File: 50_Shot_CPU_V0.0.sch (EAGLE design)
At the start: 75 parts, among them IC1 PIC24FJ128GA010, IC2 93LC46ST, J1 J12, J12 A311422_nd, J13 22-23-2021, J14 22-23-2021, J3 22-23-2021, J4 22-23-2021, J5 22-23-2021, Q1 Qs5U34CT-ND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

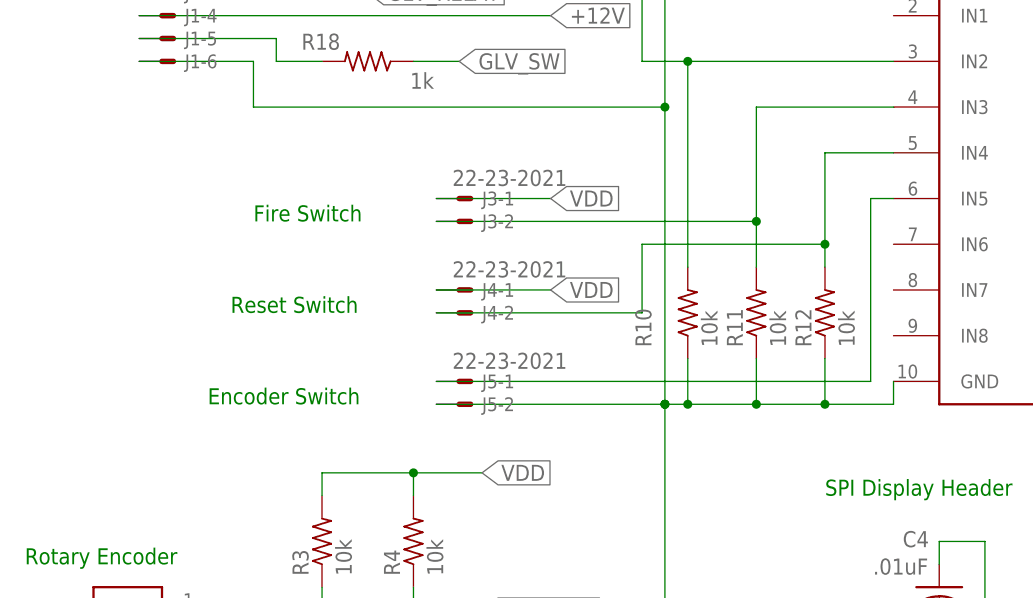
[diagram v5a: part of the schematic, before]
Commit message: Added fire/reset/encoder switches
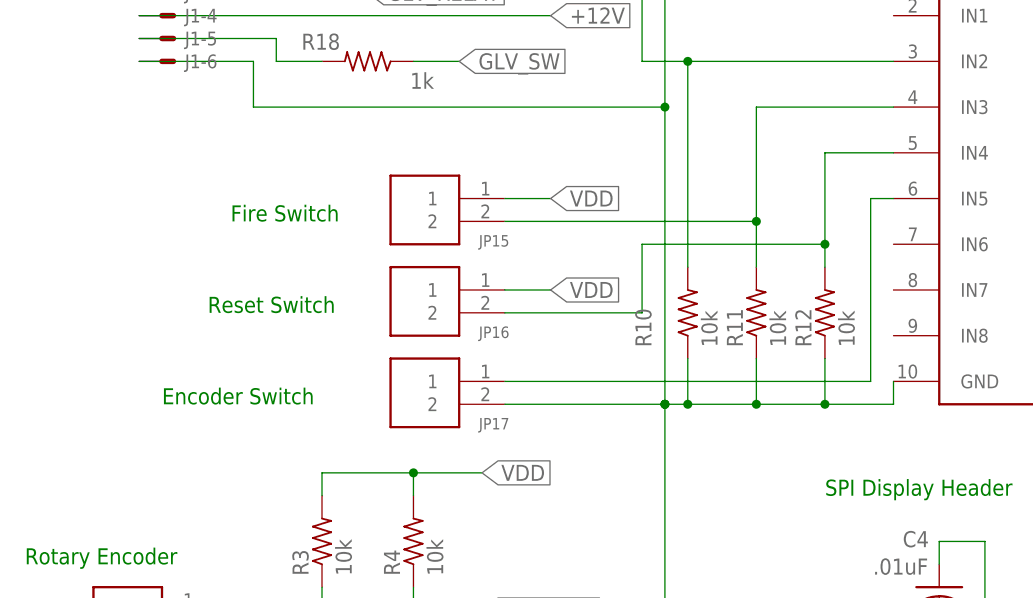
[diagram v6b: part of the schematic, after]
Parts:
- removed J3, J4, J5: 22-23-2021, Mine:22-23-2021
- added JP15, JP16, JP17: SHERLOCK_2PIN_RGT, Mine:SHERLOCK_2PIN_RGT
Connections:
- net GND: now also JP17.2; no longer J5-2.S
- net N$58: now also JP15.2; no longer J3-2.S
- net N$7: now also JP17.1; no longer J5-1.S
- net N$8: now also JP16.2; no longer J4-2.S
- net VDD: now also JP15.1, JP16.1; no longer J3-1.S, J4-1.S
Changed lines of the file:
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@@
 <part name="U1" library="Mine" deviceset="MAX6818" device="" value="MAX6818"/>
 <part name="C5" library="rcl" deviceset="C-US" device="C0805" value="1uF"/>
-<part name="J4" library="Mine" deviceset="22-23-2021" device=""/>
 <part name="R12" library="rcl" deviceset="R-US_" device="M0805" value="10k"/>
 <part name="SUPPLY4" library="supply2" deviceset="GND" device=""/>
-<part name="J5" library="Mine" deviceset="22-23-2021" device=""/>
 <part name="R11" library="rcl" deviceset="R-US_" device="M0805" value="10k"/>
 <part name="U2" library="Texas Instruments_By_element14_Batch_1" deviceset="LP2985A-33DBVTE4" device=""/>
@@
 <part name="D2" library="semicon-smd-ipc" deviceset="D-" device="SOD-80" value="LL4148FSCT-ND"/>
 <part name="SUPPLY2" library="supply2" deviceset="GND" device=""/>
-<part name="J3" library="Mine" deviceset="22-23-2021" device=""/>
 <part name="R10" library="rcl" deviceset="R-US_" device="M0805" value="10k"/>
 <part name="J12" library="Mine" deviceset="RJ_25" device="" value="A311422_nd"/>
@@
 <part name="JP13" library="Mine" deviceset="SHERLOCK_8PIN_RGT" device=""/>
 <part name="JP14" library="Mine" deviceset="SHERLOCK_6PIN_RGT" device=""/>
+<part name="JP15" library="Mine" deviceset="SHERLOCK_2PIN_RGT" device=""/>
+<part name="JP16" library="Mine" deviceset="SHERLOCK_2PIN_RGT" device=""/>
+<part name="JP17" library="Mine" deviceset="SHERLOCK_2PIN_RGT" device=""/>
 </parts>
 <sheets>
@@
 <text x="-22.86" y="86.36" size="1.778" layer="91">Circuit Board Header</text>
 <text x="-53.34" y="198.12" size="1.778" layer="91">I2C Header</text>
-<text x="-144.78" y="109.22" size="1.778" layer="91">Fire Switch</text>
-<text x="-147.32" y="99.06" size="1.778" layer="91">Reset Switch</text>
-<text x="-149.86" y="88.9" size="1.778" layer="91">Encoder Switch</text>
+<text x="-147.32" y="109.22" size="1.778" layer="91">Fire Switch</text>
+<text x="-149.86" y="99.06" size="1.778" layer="91">Reset Switch</text>
+<text x="-154.94" y="88.9" size="1.778" layer="91">Encoder Switch</text>
 <text x="-172.72" y="-17.78" size="1.778" layer="91">Firing Battery Measurement</text>
 <frame x1="-182.88" y1="-76.2" x2="276.86" y2="220.98" columns="8" rows="5" layer="91"/>
@@
 <attribute name="VALUE" x="-62.611" y="148.844" size="1.778" layer="96" rot="R270"/>
 </instance>
-<instance part="J4" gate="-1" x="-121.92" y="101.6" smashed="yes">
-<attribute name="NAME" x="-119.38" y="100.838" size="1.524" layer="95"/>
-<attribute name="VALUE" x="-122.682" y="102.997" size="1.778" layer="96"/>
-</instance>
-<instance part="J4" gate="-2" x="-121.92" y="99.06" smashed="yes">
-<attribute name="NAME" x="-119.38" y="98.298" size="1.524" layer="95"/>
-</instance>
 <instance part="R12" gate="G$1" x="-81.28" y="99.06" smashed="yes" rot="R90">
 <attribute name="NAME" x="-82.7786" y="95.25" size="1.778" layer="95" rot="R90"/>
@@
 <instance part="SUPPLY4" gate="GND" x="-99.06" y="-27.94" smashed="yes">
 <attribute name="VALUE" x="-100.965" y="-31.115" size="1.778" layer="96"/>
-</instance>
-<instance part="J5" gate="-1" x="-121.92" y="91.44" smashed="yes">
-<attribute name="NAME" x="-119.38" y="90.678" size="1.524" layer="95"/>
-<attribute name="VALUE" x="-122.682" y="92.837" size="1.778" layer="96"/>
-</instance>
-<instance part="J5" gate="-2" x="-121.92" y="88.9" smashed="yes">
-<attribute name="NAME" x="-119.38" y="88.138" size="1.524" layer="95"/>
 </instance>
 <instance part="R11" gate="G$1" x="-88.9" y="99.06" smashed="yes" rot="R90">
@@
 <attribute name="VALUE" x="-151.765" y="-8.255" size="1.778" layer="96"/>
 </instance>
-<instance part="J3" gate="-1" x="-121.92" y="111.76"/>
-<instance part="J3" gate="-2" x="-121.92" y="109.22"/>
 <instance part="R10" gate="G$1" x="-96.52" y="99.06" smashed="yes" rot="R90">
 <attribute name="NAME" x="-100.5586" y="95.25" size="1.778" layer="95" rot="R90"/>
@@
 <instance part="JP13" gate="G$1" x="238.76" y="147.32"/>
 <instance part="JP14" gate="G$1" x="238.76" y="119.38"/>
+<instance part="JP15" gate="G$1" x="-121.92" y="109.22" smashed="yes" rot="MR0">
+<attribute name="NAME" x="-116.332" y="106.426" size="1.27" layer="95" rot="MR0"/>
+</instance>
+<instance part="JP16" gate="G$1" x="-121.92" y="99.06" smashed="yes" rot="MR0">
+<attribute name="NAME" x="-116.332" y="96.266" size="1.27" layer="95" rot="MR0"/>
+</instance>
+<instance part="JP17" gate="G$1" x="-121.92" y="88.9" smashed="yes" rot="MR0">
+<attribute name="NAME" x="-116.332" y="86.106" size="1.27" layer="95" rot="MR0"/>
+</instance>
 </instances>
 <busses>
@@
 <wire x1="-99.06" y1="88.9" x2="-99.06" y2="48.26" width="0.1524" layer="91"/>
 <wire x1="-99.06" y1="48.26" x2="-99.06" y2="20.32" width="0.1524" layer="91"/>
-<pinref part="J5" gate="-2" pin="S"/>
 <wire x1="-99.06" y1="20.32" x2="-99.06" y2="10.16" width="0.1524" layer="91"/>
 <wire x1="-99.06" y1="10.16" x2="-99.06" y2="0" width="0.1524" layer="91"/>
@@
 <wire x1="-99.06" y1="-10.16" x2="-99.06" y2="-20.32" width="0.1524" layer="91"/>
 <wire x1="-99.06" y1="-20.32" x2="-99.06" y2="-25.4" width="0.1524" layer="91"/>
-<wire x1="-124.46" y1="88.9" x2="-99.06" y2="88.9" width="0.1524" layer="91"/>
+<wire x1="-116.84" y1="88.9" x2="-99.06" y2="88.9" width="0.1524" layer="91"/>
 <junction x="-99.06" y="88.9"/>
 <wire x1="-73.66" y1="88.9" x2="-81.28" y2="88.9" width="0.1524" layer="91"/>
@@
 <wire x1="-114.3" y1="-20.32" x2="-99.06" y2="-20.32" width="0.1524" layer="91"/>
 <junction x="-99.06" y="-20.32"/>
+<pinref part="JP17" gate="G$1" pin="2"/>
 </segment>
 <segment>
@@
 </segment>
 <segment>
-<pinref part="J4" gate="-1" pin="S"/>
-<wire x1="-124.46" y1="101.6" x2="-111.76" y2="101.6" width="0.1524" layer="91"/>
+<wire x1="-116.84" y1="101.6" x2="-111.76" y2="101.6" width="0.1524" layer="91"/>
 <label x="-111.76" y="101.6" size="1.778" layer="95" xref="yes"/>
-</segment>
-<segment>
-<pinref part="J3" gate="-1" pin="S"/>
-<wire x1="-124.46" y1="111.76" x2="-111.76" y2="111.76" width="0.1524" layer="91"/>
+<pinref part="JP16" gate="G$1" pin="1"/>
+</segment>
+<segment>
+<wire x1="-116.84" y1="111.76" x2="-111.76" y2="111.76" width="0.1524" layer="91"/>
 <label x="-111.76" y="111.76" size="1.778" layer="95" xref="yes"/>
+<pinref part="JP15" gate="G$1" pin="1"/>
 </segment>
 <segment>
@@
 <net name="N$8" class="0">
 <segment>
-<pinref part="J4" gate="-2" pin="S"/>
-<wire x1="-124.46" y1="99.06" x2="-101.6" y2="99.06" width="0.1524" layer="91"/>
+<wire x1="-116.84" y1="99.06" x2="-101.6" y2="99.06" width="0.1524" layer="91"/>
 <wire x1="-101.6" y1="99.06" x2="-101.6" y2="106.68" width="0.1524" layer="91"/>
 <pinref part="R12" gate="G$1" pin="2"/>
@@
 <wire x1="-101.6" y1="106.68" x2="-81.28" y2="106.68" width="0.1524" layer="91"/>
 <junction x="-81.28" y="106.68"/>
+<pinref part="JP16" gate="G$1" pin="2"/>
 </segment>
 </net>
@@
 <net name="N$7" class="0">
 <segment>
-<pinref part="J5" gate="-1" pin="S"/>
-<wire x1="-124.46" y1="91.44" x2="-76.2" y2="91.44" width="0.1524" layer="91"/>
+<wire x1="-116.84" y1="91.44" x2="-76.2" y2="91.44" width="0.1524" layer="91"/>
 <wire x1="-76.2" y1="91.44" x2="-76.2" y2="111.76" width="0.1524" layer="91"/>
 <pinref part="U1" gate="MAX6818" pin="IN5"/>
 <wire x1="-76.2" y1="111.76" x2="-73.66" y2="111.76" width="0.1524" layer="91"/>
+<pinref part="JP17" gate="G$1" pin="1"/>
 </segment>
 </net>
@@
 <net name="N$58" class="0">
 <segment>
-<pinref part="J3" gate="-2" pin="S"/>
 <pinref part="U1" gate="MAX6818" pin="IN3"/>
 <wire x1="-73.66" y1="121.92" x2="-88.9" y2="121.92" width="0.1524" layer="91"/>
@@
 <wire x1="-88.9" y1="121.92" x2="-88.9" y2="109.22" width="0.1524" layer="91"/>
 <wire x1="-88.9" y1="109.22" x2="-88.9" y2="104.14" width="0.1524" layer="91"/>
-<wire x1="-124.46" y1="109.22" x2="-88.9" y2="109.22" width="0.1524" layer="91"/>
+<wire x1="-116.84" y1="109.22" x2="-88.9" y2="109.22" width="0.1524" layer="91"/>
 <junction x="-88.9" y="109.22"/>
-</segment>
-</net>
+<pinref part="JP15" gate="G$1" pin="2"/>
+</segment>
+</net>
